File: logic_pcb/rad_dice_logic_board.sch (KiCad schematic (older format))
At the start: 16 parts, among them J1 SAMPLE-GEIGER-CONNECTOR, J2 NIXIE-CONNECTOR-CS, J3 NIXIE-CONNECTOR-SCK-MOSI, J4 SWITCH-CONNECTOR, J5 POWER-5V, J6 GROUND, J7 TOGGLE-CONNECTOR, U1 ADAFRUIT-DS3231

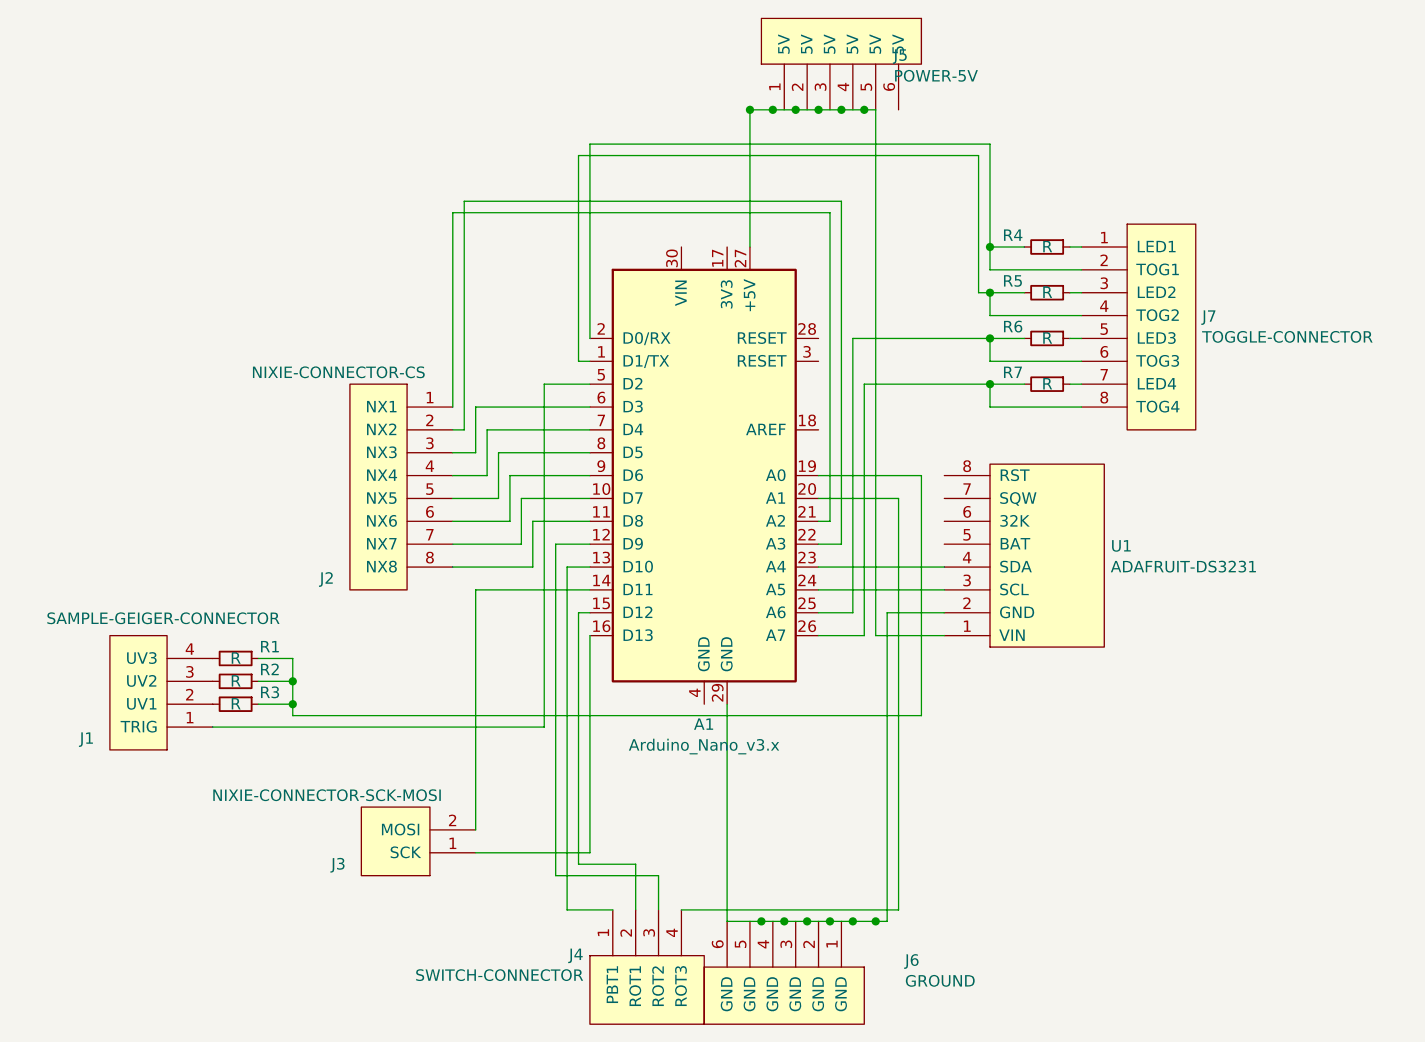
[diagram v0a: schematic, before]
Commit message: update logic board for compatibility with front panel board
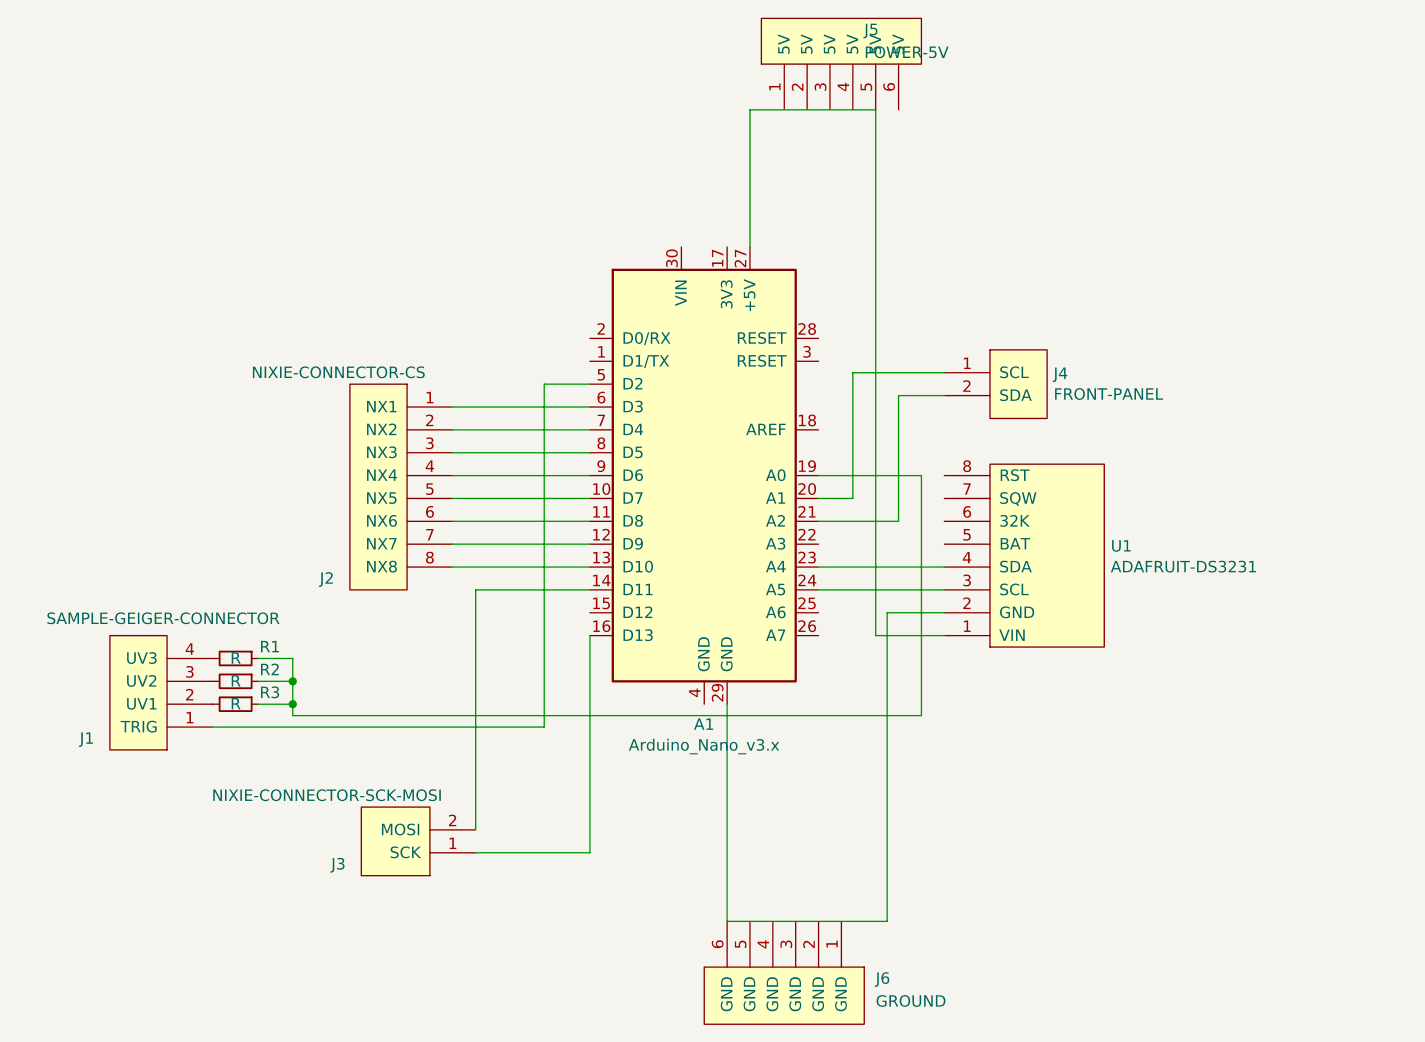
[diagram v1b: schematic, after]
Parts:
- removed J4: SWITCH-CONNECTOR, Pin_Headers:Pin_Header_Angled_1x04_Pitch2.54mm, symbol rad_dice_logic_board:SWITCH-CONNECTOR
- removed J7: TOGGLE-CONNECTOR, Pin_Headers:Pin_Header_Angled_2x04_Pitch2.54mm, symbol rad_dice_logic_board:TOGGLE-CONNECTOR
- removed R4, R5, R6, R7: R, Resistors_THT:R_Axial_DIN0207_L6.3mm_D2.5mm_P10.16mm_Horizontal, symbol Device:R_Small
- added J4: FRONT-PANEL, Pin_Headers:Pin_Header_Angled_1x02_Pitch2.54mm, symbol rad_dice_logic_board:FRONT-PANEL
- J5, J6: footprint Pin_Headers:Pin_Header_Angled_2x03_Pitch2.54mm -> Pin_Headers:Pin_Header_Angled_1x03_Pitch2.54mm
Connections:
- net at A1.10 (D7): now also J2.5 (NX5); no longer J2.7 (NX7)
- net at A1.11 (D8): now also J2.6 (NX6); no longer J2.8 (NX8)
- net at A1.12 (D9): now also J2.7 (NX7)
- net at A1.13 (D10): now also J2.8 (NX8)
- net at A1.20 (A1): now also J4.1 (SCL)
- net at A1.21 (A2): now also J4.2 (SDA); no longer J2.1 (NX1)
- net at A1.22 (A3): no longer J2.2 (NX2)
- net at A1.6 (D3): now also J2.1 (NX1); no longer J2.3 (NX3)
- net at A1.7 (D4): now also J2.2 (NX2); no longer J2.4 (NX4)
- net at A1.8 (D5): now also J2.3 (NX3); no longer J2.5 (NX5)
- net at A1.9 (D6): now also J2.4 (NX4); no longer J2.6 (NX6)

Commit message: fix gnd/5v bug and add 2 gpio pins
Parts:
- added J7: GPIO, Pin_Headers:Pin_Header_Angled_1x02_Pitch2.54mm, symbol rad_dice_logic_board:GPIO
- J5, J6: footprint Pin_Headers:Pin_Header_Angled_1x03_Pitch2.54mm -> Pin_Headers:Pin_Header_Angled_1x06_Pitch2.54mm
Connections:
- net at A1.15 (D12): now also J7.1 (IO1)
- net at A1.22 (A3): now also J7.2 (IO2)
- net at A1.27 (+5V), J5.5 (5V), U1.1 (VIN): now also J5.1 (5V), J5.2 (5V), J5.3 (5V), J5.4 (5V), J5.6 (5V)
- net at A1.29 (GND), J6.6 (GND), U1.2 (GND): now also J6.1 (GND), J6.2 (GND), J6.3 (GND), J6.4 (GND), J6.5 (GND)
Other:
- moved on the sheet: J5
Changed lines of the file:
@@
 F 0 "J6" H 3700 5800 50  0000 R CNN
 F 1 "GROUND" H 3700 5900 50  0000 R CNN
-F 2 "Pin_Headers:Pin_Header_Angled_1x03_Pitch2.54mm" H 4000 5750 50  0001 C CNN
+F 2 "Pin_Headers:Pin_Header_Angled_1x06_Pitch2.54mm" H 4000 5750 50  0001 C CNN
 F 3 "" H 4000 5750 50  0001 C CNN
 	1    3950 5750
@@
 	4400 3600 4400 4650
 Connection ~ 1650 4600
-$Comp
-L rad_dice_logic_board:POWER-5V J5
-U 1 1 5D1FDF4F
-P 3900 1800
-F 0 "J5" H 4150 1950 50  0000 L CNN
-F 1 "POWER-5V" H 4150 1850 50  0000 L CNN
-F 2 "Pin_Headers:Pin_Header_Angled_1x03_Pitch2.54mm" H 3950 1800 50  0001 C CNN
-F 3 "" H 3950 1800 50  0001 C CNN
-	1    3900 1800
-	1    0    0    -1
-$EndComp
 Wire Wire Line
 	4250 4200 4250 5550
@@
 Wire Wire Line
 	4300 3250 4500 3250
-Wire Wire Line
-	3650 2000 4200 2000
-Wire Wire Line
-	3550 5550 4250 5550
+$Comp
+L rad_dice_logic_board:POWER-5V J5
+U 1 1 5D1FDF4F
+P 3800 1800
+F 0 "J5" H 4050 1950 50  0000 L CNN
+F 1 "POWER-5V" H 4050 1850 50  0000 L CNN
+F 2 "Pin_Headers:Pin_Header_Angled_1x06_Pitch2.54mm" H 3850 1800 50  0001 C CNN
+F 3 "" H 3850 1800 50  0001 C CNN
+	1    3800 1800
+	1    0    0    -1
+$EndComp
+Wire Wire Line
+	3650 2000 3700 2000
+Wire Wire Line
+	3700 2000 3800 2000
+Connection ~ 3700 2000
+Connection ~ 4200 2000
+Connection ~ 3800 2000
+Wire Wire Line
+	3800 2000 3900 2000
+Connection ~ 3900 2000
+Wire Wire Line
+	3900 2000 4000 2000
+Connection ~ 4000 2000
+Wire Wire Line
+	4000 2000 4100 2000
+Connection ~ 4100 2000
+Wire Wire Line
+	4100 2000 4200 2000
+Wire Wire Line
+	4250 5550 4050 5550
+Connection ~ 3550 5550
+Connection ~ 3650 5550
+Wire Wire Line
+	3650 5550 3550 5550
+Connection ~ 3750 5550
+Wire Wire Line
+	3750 5550 3650 5550
+Connection ~ 3850 5550
+Wire Wire Line
+	3850 5550 3750 5550
+Connection ~ 3950 5550
+Wire Wire Line
+	3950 5550 3850 5550
+Connection ~ 4050 5550
+Wire Wire Line
+	4050 5550 3950 5550
+$Comp
+L rad_dice_logic_board:GPIO J7
+U 1 1 5D877BB1
+P 4700 5050
+F 0 "J7" V 4654 5328 50  0000 L CNN
+F 1 "GPIO" V 4745 5328 50  0000 L CNN
+F 2 "Pin_Headers:Pin_Header_Angled_1x02_Pitch2.54mm" H 4700 5050 50  0001 C CNN
+F 3 "" H 4700 5050 50  0001 C CNN
+	1    4700 5050
+	0    1    1    0
+$EndComp
+Wire Wire Line
+	2950 4200 2850 4200
+Wire Wire Line
+	2850 4200 2850 5000
+Wire Wire Line
+	2850 5000 4500 5000
+Wire Wire Line
+	3950 3900 4150 3900
+Wire Wire Line
+	4150 3900 4150 5100
+Wire Wire Line
+	4150 5100 4500 5100
 $EndSCHEMATC
